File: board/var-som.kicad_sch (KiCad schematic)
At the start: 19 parts, among them U1 VAR-SOM

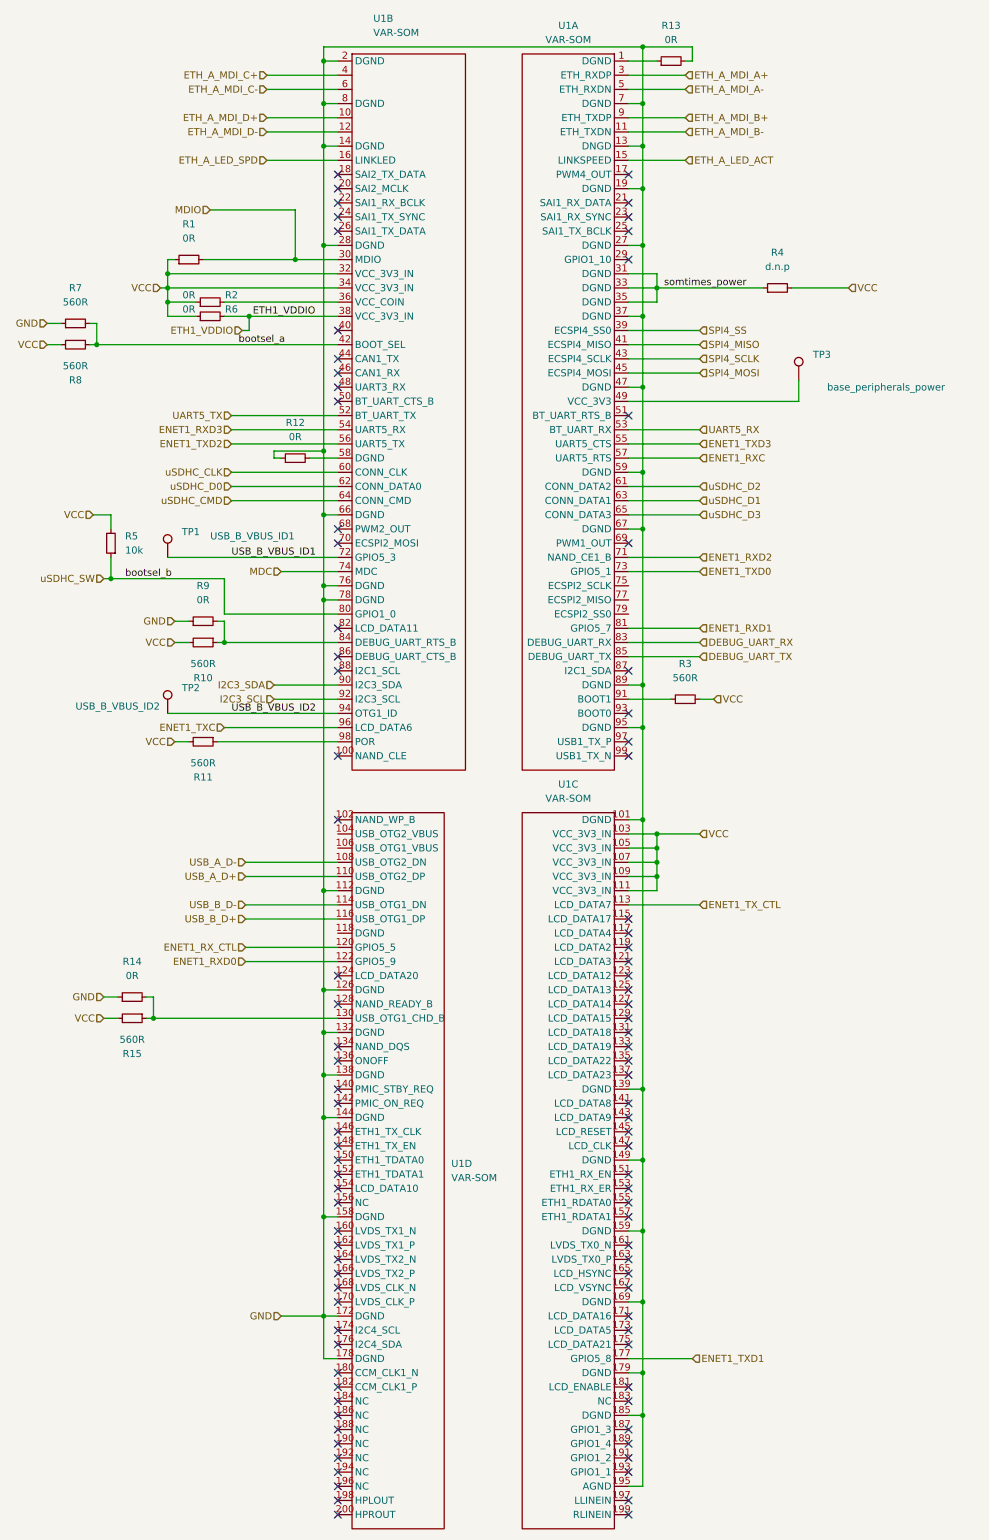
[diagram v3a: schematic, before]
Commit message: Update PU/PDn and values
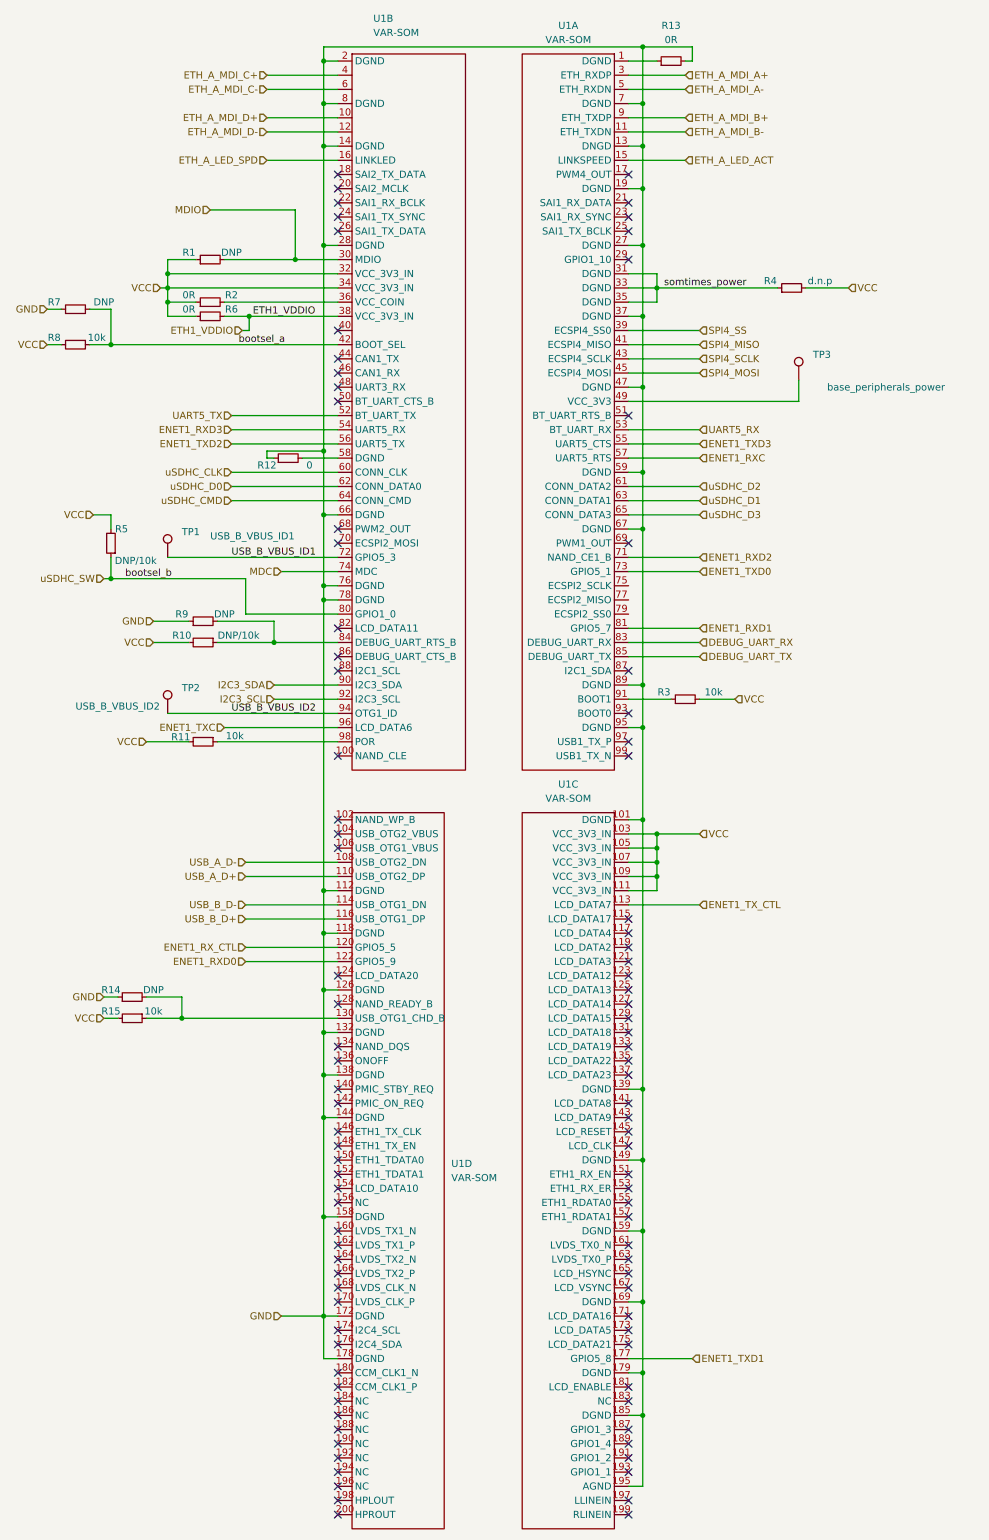
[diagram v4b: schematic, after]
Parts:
- R1, R14, R9: value 0R -> DNP
- R10: value 560R -> DNP/10k
- R11, R15, R3, R8: value 560R -> 10k
- R12: value 0R -> 0
- R5: value 10k -> DNP/10k
- R7: value 560R -> DNP
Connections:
- net GND: now also U1.118 (DGND)
- no-connect marks 94 -> 96
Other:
- moved on the sheet: R1, R12, R4, R7
